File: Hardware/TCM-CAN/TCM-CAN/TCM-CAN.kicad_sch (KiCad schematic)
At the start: 1 part, among them J1 DTM13-12PA

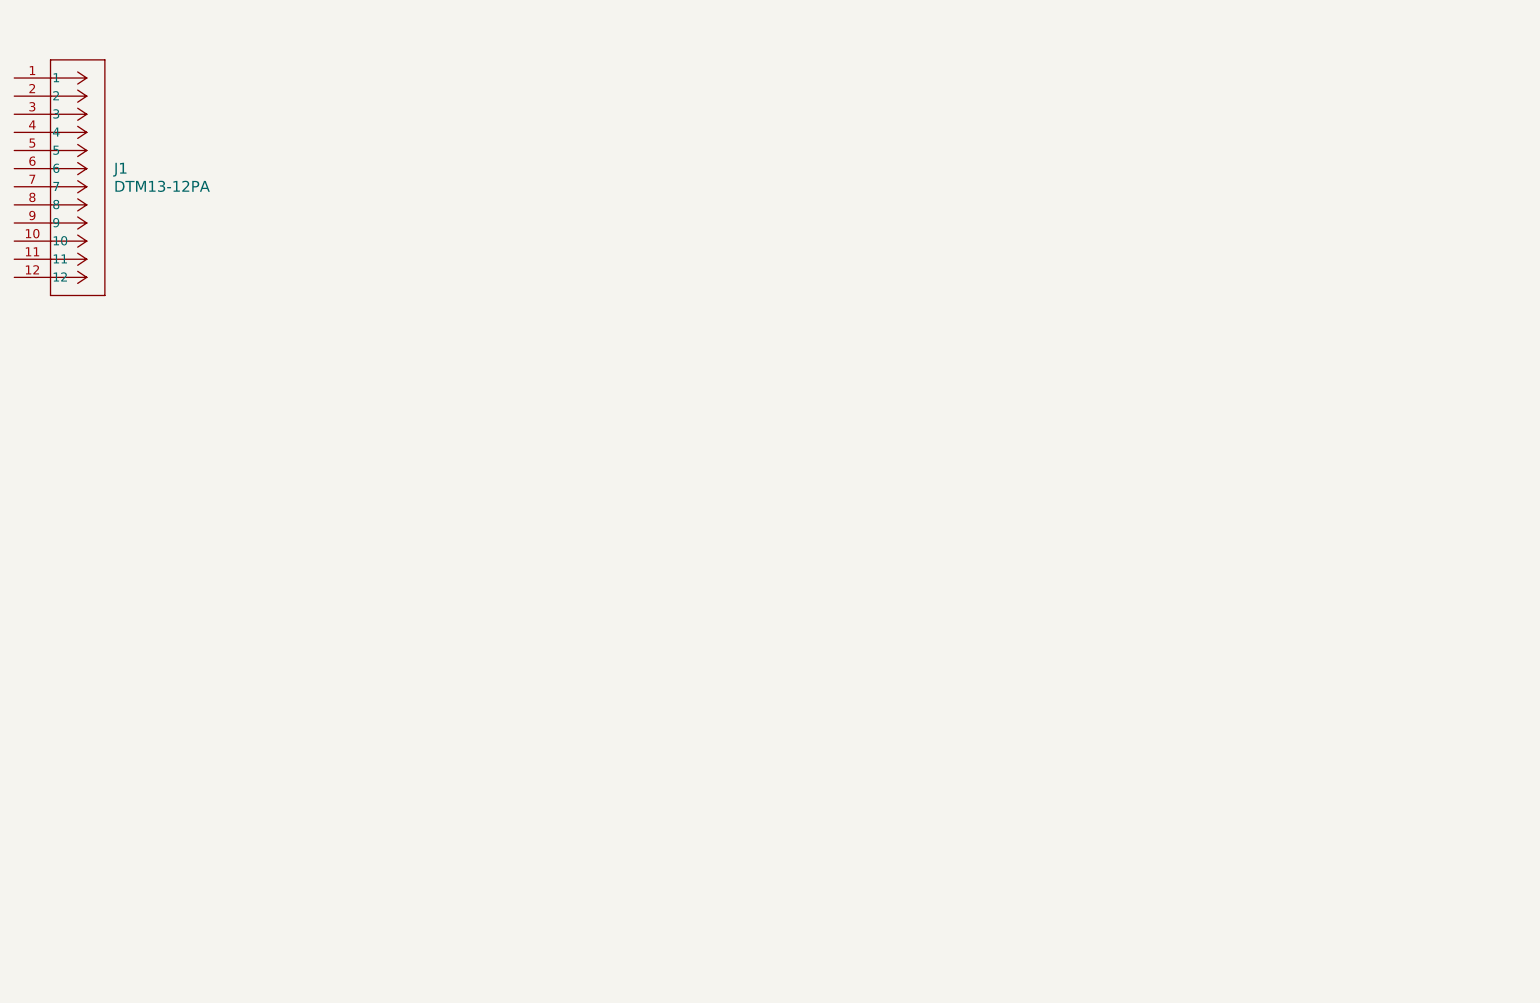
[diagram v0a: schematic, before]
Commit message: tcm can schematic done, only needs to be routed
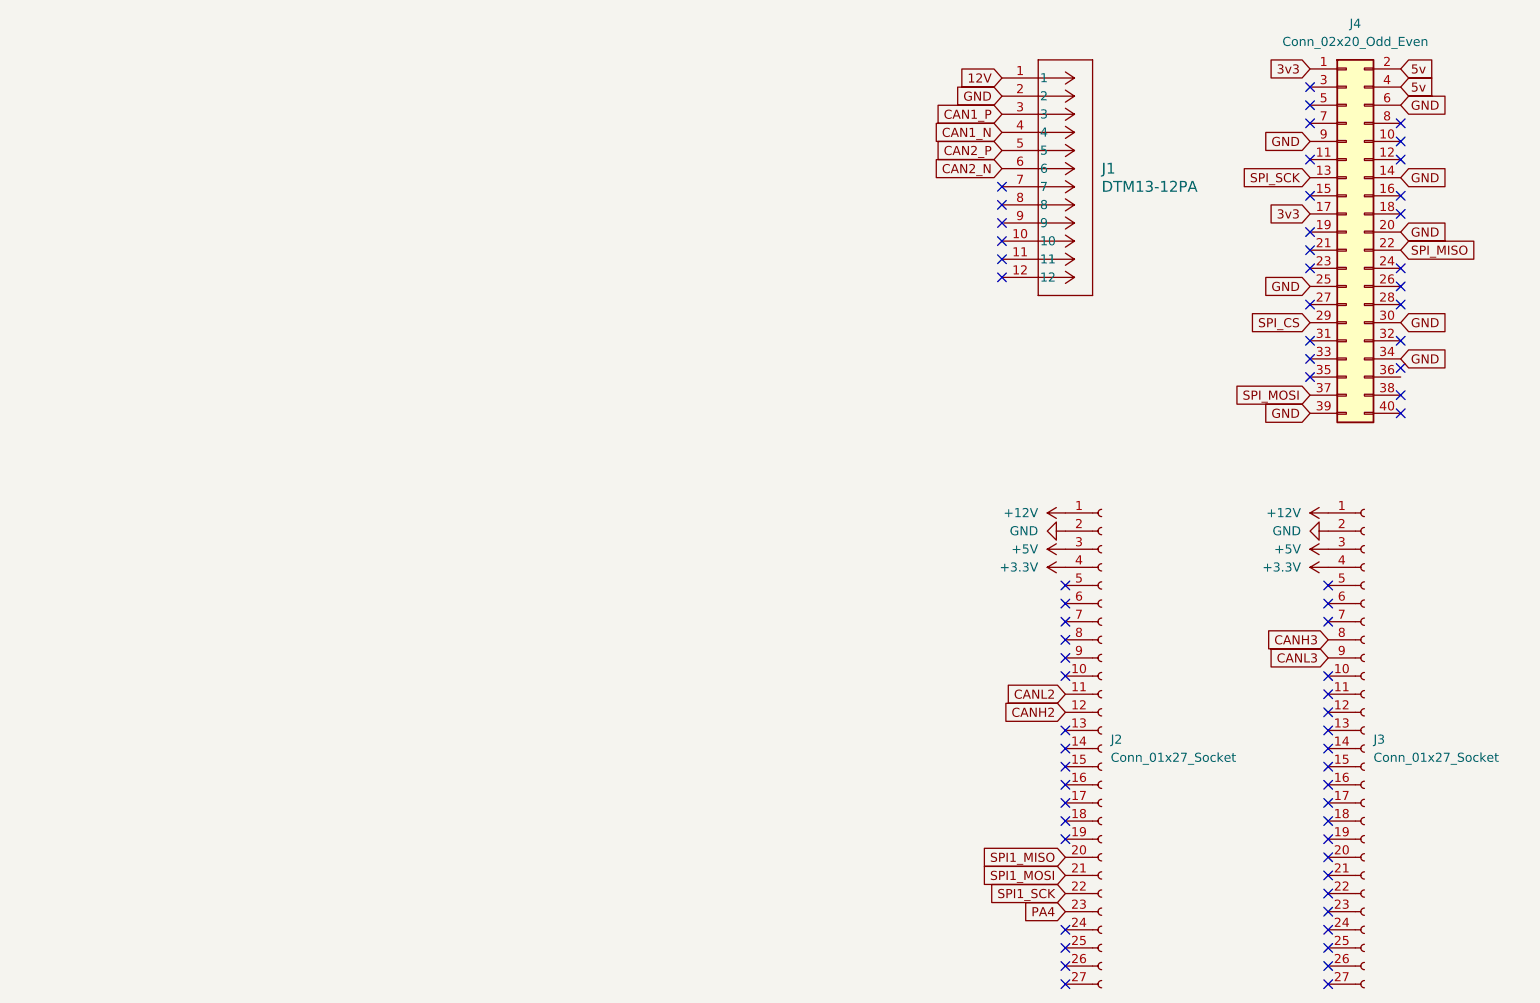
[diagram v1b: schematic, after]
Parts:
- added J2, J3: Conn_01x27_Socket, Connector_PinHeader_2.54mm:PinHeader_1x27_P2.54mm_Vertical, symbol Connector:Conn_01x27_Socket
- added J4: Conn_02x20_Odd_Even, Connector_PinSocket_2.54mm:PinSocket_2x20_P2.54mm_Vertical, symbol Connector_Generic:Conn_02x20_Odd_Even
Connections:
- net 12V: now reaches J1.1
- net GND: now reaches J1.2
- net GND: now also J2.2 (Pin_2), J3.2 (Pin_2), J4.14 (Pin_14), J4.20 (Pin_20), J4.25 (Pin_25), J4.30 (Pin_30), J4.34 (Pin_34), J4.39 (Pin_39), J4.6 (Pin_6), J4.9 (Pin_9)
- net CAN1_P: now reaches J1.3
- net CAN1_N: now reaches J1.4
- net CAN2_P: now reaches J1.5
- net CAN2_N: now reaches J1.6
- new net +12V: J2.1 (Pin_1), J3.1 (Pin_1)
- new net +3.3V: J2.4 (Pin_4), J3.4 (Pin_4)
- new net +5V: J2.3 (Pin_3), J3.3 (Pin_3)
- new net 3v3: J4.1 (Pin_1), J4.17 (Pin_17)
- new net 5v: J4.2 (Pin_2), J4.4 (Pin_4)
- new net CANH2: J2.12 (Pin_12)
- new net CANH3: J3.8 (Pin_8)
- new net CANL2: J2.11 (Pin_11)
- new net CANL3: J3.9 (Pin_9)
- new net PA4: J2.23 (Pin_23)
- new net SPI1_MISO: J2.20 (Pin_20)
- new net SPI1_MOSI: J2.21 (Pin_21)
- new net SPI1_SCK: J2.22 (Pin_22)
- new net SPI_CS: J4.29 (Pin_29)
- new net SPI_MISO: J4.22 (Pin_22)
- new net SPI_MOSI: J4.37 (Pin_37)
- new net SPI_SCK: J4.13 (Pin_13)
- no-connect marks 0 -> 68
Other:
- moved on the sheet: J1

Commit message: bug fix
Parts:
- removed J1: DTM13-12PA, CONN12_DTM13-12PA_TEC, symbol DTM:DTM13-12PA
- added J5: Conn_01x06_Socket, Connector_JST:JST_XH_B6B-XH-A_1x06_P2.50mm_Vertical, symbol Connector:Conn_01x06_Socket
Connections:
- net 12V: now also J5.1 (Pin_1)
- net CAN1_N: now also J5.4 (Pin_4)
- net CAN1_P: now also J5.3 (Pin_3)
- net CAN2_N: now also J5.6 (Pin_6)
- net CAN2_P: now also J5.5 (Pin_5)
- net GND: now also J5.2 (Pin_2)
- no-connect marks 68 -> 62
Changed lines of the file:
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@@
 	)
 	(no_connect
-		(at 171.45 36.83)
-	)
-	(no_connect
 		(at 227.33 62.23)
 	)
@@
 	)
 	(no_connect
-		(at 171.45 49.53)
-	)
-	(no_connect
 		(at 180.34 125.73)
 	)
@@
 	)
 	(no_connect
-		(at 171.45 41.91)
-	)
-	(no_connect
 		(at 217.17 113.03)
 	)
@@
 	)
 	(no_connect
-		(at 171.45 44.45)
-	)
-	(no_connect
 		(at 214.63 27.94)
 	)
@@
 	)
 	(no_connect
-		(at 171.45 39.37)
-	)
-	(no_connect
 		(at 227.33 38.1)
 	)
 	(no_connect
-		(at 171.45 46.99)
-	)
-	(no_connect
 		(at 217.17 138.43)
 	)
@@
 			"AAAAAAAAAAAAAAAAAAAAAAAAAAAAAAAAAAAAAAAAAAAAAAAAAAAAAAAAAAAAAAAAAAAAAAAAAAAA"
 			"AAAAAAAAAAAAAAAAAAAAAAAAAAAAAAAAAAAAAAAAAAAAAAAAAAAAAAAAAAAAAAAAAAAAAAAAAAAA"
-			"AAAAAAAAAAAAAAAAAAAAAAAAAAAAAAAAAAAAAAA="
+			"AAAAAAAAAAAAAAAAAAAAAAAAAAAAAAAAAAAAAAAAAAAAAAAAAAAAAAAAAAAAAAAAAAAAAAAAAAAA"
+			"AAAAAAAAAAAAAAAAAAAAAAAAAAAAAAAAAAAAAAAAAAAAAAAAAAAAAAAAAAAAAAAAAAAAAAAAAAAA"
+			"AAAAAAAAAAAAAAAAAAAAAAAAAAAAAAAAAAAAAAAAAAAAAAAAAAAAAAAAAAAAAAAAAAAAAAAAAAAA"
+			"AAAAAAAAAAAAAAAAAAAAAAAAAAAAAAAAAAAAAAAAAAAAAAAAAAAAAAAAAAAAAAAAAAAAAAAAAAAA"
+			"AAAAAAAAAAAAAAAAAAAAAAAAAAAAAAAAAAAAAAAAAAAAAAAAAAAAAAAAAAAAAAAAAAAAAAAAAAAA"
+			"AAAAAAAAAAAAAAAAAAAAAAAAAAAAAAAAAAAAAAAAAAAAAAAAAAAAAAAAAAAAAAAAAAAAAAAAAAAA"
+			"AAAAAAAAAAAAAAAAAAAAAAAAAAAAAAAAAAAAAAAAAAAAAAAAAAAAAAAAAAAAAAAAAAAAAAAAAAAA"
+			"AAAAAAAAAAAAAAAAAAAAAAAAAAAAAAAAAAAAAAAAAAAAAAAAAAAAAAAAAAAAAAAAAAAAAAAAAAAA"
+			"AAAAAAAAAAAAAAAAAAAAAAAAAAAAAAAAAAAAAAAAAAAAAAAAAAAAAAAAAAAAAAAAAAAAAAAAAAAA"
+			"AAAAAAAAAAAAAAAAAAAAAAAAAAAAAAAAAAAAAAAAAAAAAAAAAAAAAAAAAAAAAAAAAAAAAAAAAAAA"
+			"AAAAAAAAAAAAAAAAAAAAAAAAAAAAAAAAAAAAAAAAAAAAAAAAAAAAAAAAAAAAAAAAAAAAAAAAAAAA"
+			"AAAAAAAAAAAAAAAAAAAAAAAAAAAAAAAAAAAAAAAAAAAAAAAAAAAAAAAAAAAAAAAAAAAAAAAAAAAA"
+			"AAAAAAAAAAAAAAAAAAAAAAAAAAAAAAAAAAAAAAAAAAAAAAAAAAAAAAAAAAAAAAAAAAAAAAAAAAAA"
+			"AAAAAAAAAAAAAAAAAAAAAAAAAAAAAAAAAAAAAAAAAAAAAAAAAAAAAAAAAAAAAAAAAAAAAAAAAAAA"
+			"AAAAAAAAAAAAAAAAAAAAAAAAAAAAAAAAAAAAAAAAAAAAAAAAAAAAAAAAAAAAAAAAAAAAAAAAAAAA"
+			"AAAAAAAAAAAAAAAAAAAAAAAAAAAAAAAAAAAAAAAAAAAAAAAAAAAAAAAAAAAAAAAAAAAAAAAAAAAA"
+			"AAAAAAAAAAAAAAAAAAAAAAAAAAAAAAAAAAAAAAAAAAAAAAAAAAAAAAAAAAAAAAAAAAAAAAAAAAAA"
+			"AAAAAAAAAAAAAAAAAAAAAAAAAAAAAAAAAAAAAAAAAAAAAAAAAAAAAAAAAAAAAAAAAAAAAAAAAAAA"
+			"AAAAAAAAAAAAAAAAAAAAAAAAAAAAAAAAAAAAAA=="
 		)
 	)
@@
 		)
 	)
-	(global_label "3v3"
+	(global_label "CAN2_N"
 		(shape input)
-		(at 214.63 40.64 180)
+		(at 162.56 71.12 180)
 		(fields_autoplaced yes)
 		(effects
@@
 		)
 		(property "Intersheetrefs" "${INTERSHEET_REFS}"
-			(at 208.2582 40.64 0)
+			(at 152.3781 71.12 0)
 			(effects
 				(font
@@
 		)
 	)
-	(global_label "12V"
+	(global_label "CAN1_P"
+		(shape input)
+		(at 162.56 63.5 180)
+		(fields_autoplaced yes)
+		(effects
+			(font
+				(size 1.27 1.27)
+			)
+			(justify right)
+		)
+		(property "Intersheetrefs" "${INTERSHEET_REFS}"
+			(at 152.4386 63.5 0)
+			(effects
+				(font
+					(size 1.27 1.27)
+				)
+				(justify right)
+				(hide yes)
+			)
+		)
+	)
+	(global_label "3v3"
 		(shape input)
-		(at 171.45 21.59 180)
+		(at 214.63 40.64 180)
 		(fields_autoplaced yes)
 		(effects
@@
 		)
 		(property "Intersheetrefs" "${INTERSHEET_REFS}"
-			(at 164.9572 21.59 0)
+			(at 208.2582 40.64 0)
 			(effects
 				(font
@@
 	(global_label "GND"
 		(shape input)
-		(at 171.45 24.13 180)
+		(at 162.56 60.96 180)
 		(fields_autoplaced yes)
 		(effects
@@
 		)
 		(property "Intersheetrefs" "${INTERSHEET_REFS}"
-			(at 164.5943 24.13 0)
+			(at 155.7043 60.96 0)
 			(effects
 				(font
@@
 		)
 	)
-	(global_label "CAN2_P"
-		(shape input)
-		(at 171.45 31.75 180)
-		(fields_autoplaced yes)
-		(effects
-			(font
-				(size 1.27 1.27)
-			)
-			(justify right)
-		)
-		(property "Intersheetrefs" "${INTERSHEET_REFS}"
-			(at 161.3286 31.75 0)
-			(effects
-				(font
-					(size 1.27 1.27)
-				)
-				(justify right)
-				(hide yes)
-			)
-		)
-	)
 	(global_label "SPI_MOSI"
 		(shape input)
@@
 		)
 	)
-	(global_label "CAN1_P"
-		(shape input)
-		(at 171.45 26.67 180)
-		(fields_autoplaced yes)
-		(effects
-			(font
-				(size 1.27 1.27)
-			)
-			(justify right)
-		)
-		(property "Intersheetrefs" "${INTERSHEET_REFS}"
-			(at 161.3286 26.67 0)
-			(effects
-				(font
-					(size 1.27 1.27)
-				)
-				(justify right)
-				(hide yes)
-			)
-		)
-	)
-	(global_label "CAN2_N"
+	(global_label "CAN1_N"
 		(shape input)
-		(at 171.45 34.29 180)
+		(at 162.56 66.04 180)
 		(fields_autoplaced yes)
 		(effects
@@
 		)
 		(property "Intersheetrefs" "${INTERSHEET_REFS}"
-			(at 161.2681 34.29 0)
+			(at 152.3781 66.04 0)
 			(effects
 				(font
@@
 		)
 	)
-	(global_label "CAN1_N"
+	(global_label "PA4"
 		(shape input)
-		(at 171.45 29.21 180)
+		(at 180.34 138.43 180)
 		(fields_autoplaced yes)
 		(effects
@@
 		)
 		(property "Intersheetrefs" "${INTERSHEET_REFS}"
-			(at 161.2681 29.21 0)
+			(at 173.7867 138.43 0)
 			(effects
 				(font
@@
 		)
 	)
-	(global_label "PA4"
+	(global_label "SPI1_SCK"
 		(shape input)
-		(at 180.34 138.43 180)
+		(at 180.34 135.89 180)
 		(fields_autoplaced yes)
 		(effects
@@
 		)
 		(property "Intersheetrefs" "${INTERSHEET_REFS}"
-			(at 173.7867 138.43 0)
+			(at 168.3439 135.89 0)
 			(effects
 				(font
@@
 		)
 	)
-	(global_label "SPI1_SCK"
+	(global_label "CAN2_P"
 		(shape input)
-		(at 180.34 135.89 180)
+		(at 162.56 68.58 180)
 		(fields_autoplaced yes)
 		(effects
@@
 		)
 		(property "Intersheetrefs" "${INTERSHEET_REFS}"
-			(at 168.3439 135.89 0)
+			(at 152.4386 68.58 0)
 			(effects
 				(font
@@
 		)
 	)
-	(global_label "GND"
+	(global_label "12V"
 		(shape input)
-		(at 214.63 30.48 180)
+		(at 162.56 58.42 180)
 		(fields_autoplaced yes)
 		(effects
@@
 		)
 		(property "Intersheetrefs" "${INTERSHEET_REFS}"
-			(at 207.7743 30.48 0)
+			(at 156.0672 58.42 0)
 			(effects
 				(font
@@
 	(global_label "GND"
 		(shape input)
-		(at 227.33 43.18 0)
+		(at 214.63 30.48 180)
 		(fields_autoplaced yes)
 		(effects
@@
 				(size 1.27 1.27)
 			)
-			(justify left)
+			(justify right)
 		)
 		(property "Intersheetrefs" "${INTERSHEET_REFS}"
-			(at 234.1857 43.18 0)
+			(at 207.7743 30.48 0)
 			(effects
 				(font
 					(size 1.27 1.27)
 				)
-				(justify left)
+				(justify right)
 				(hide yes)
 			)
 		)
 	)
-	(symbol
-		(lib_id "DTM:DTM13-12PA")
-		(at 181.61 36.83 0)
-		(unit 1)
-		(exclude_from_sim no)
-		(in_bom yes)
-		(on_board yes)
-		(dnp no)
+	(global_label "GND"
+		(shape input)
+		(at 227.33 43.18 0)
 		(fields_autoplaced yes)
-		(property "Reference" "J1"
-			(at 185.42 34.2899 0)
-			(effects
-				(font
-					(size 1.524 1.524)
-				)
-				(justify left)
-			)
-		)
-		(property "Value" "DTM13-12PA"
-			(at 185.42 36.8299 0)
-			(effects
-				(font
-					(size 1.524 1.524)
-				)
-				(justify left)
-			)
-		)
-		(property "Footprint" "CONN12_DTM13-12PA_TEC"
-			(at 181.61 36.83 0)
-			(effects
-				(font
-					(size 1.27 1.27)
-					(italic yes)
-				)
-				(hide yes)
-			)
-		)
-		(property "Datasheet" "DTM13-12PA"
-			(at 181.61 36.83 0)
-			(effects
-				(font
-					(size 1.27 1.27)
-					(italic yes)
-				)
-				(hide yes)
+		(effects
+			(font
+				(size 1.27 1.27)
 			)
+			(justify left)
 		)
-		(property "Description" ""
-			(at 181.61 36.83 0)
+		(property "Intersheetrefs" "${INTERSHEET_REFS}"
+			(at 234.1857 43.18 0)
 			(effects
 				(font
 					(size 1.27 1.27)
 				)
+				(justify left)
 				(hide yes)
 			)
 		)
-		(pin "8"
-		)
-		(pin "3"
-		)
-		(pin "6"
-		)
-		(pin "4"
-		)
-		(pin "1"
-		)
-		(pin "12"
-		)
-		(pin "10"
-		)
-		(pin "5"
-		)
-		(pin "9"
-		)
-		(pin "2"
-		)
-		(pin "7"
-		)
-		(pin "11"
-		)
-		(instances
-			(project ""
-				(path "/dce5d582-08ac-45e6-8e98-75b83df6efb2"
-					(reference "J1")
-					(unit 1)
-				)
-			)
-		)
 	)
 	(symbol
@@
 					(unit 1)
 				)
+			)
+		)
+	)
+	(symbol
+		(lib_id "Connector:Conn_01x06_Socket")
+		(at 167.64 63.5 0)
+		(unit 1)
+		(exclude_from_sim no)
+		(in_bom yes)
+		(on_board yes)
+		(dnp no)
+		(fields_autoplaced yes)
+		(property "Reference" "J5"
+			(at 168.91 63.4999 0)
+			(effects
+				(font
+					(size 1.27 1.27)
+				)
+				(justify left)
+			)
+		)
+		(property "Value" "Conn_01x06_Socket"
+			(at 168.91 66.0399 0)
+			(effects
+				(font
+					(size 1.27 1.27)
+				)
+				(justify left)
+			)
+		)
+		(property "Footprint" "Connector_JST:JST_XH_B6B-XH-A_1x06_P2.50mm_Vertical"
+			(at 167.64 63.5 0)
+			(effects
+				(font
+					(size 1.27 1.27)
+				)
+				(hide yes)
+			)
+		)
+		(property "Datasheet" "~"
+			(at 167.64 63.5 0)
+			(effects
+				(font
+					(size 1.27 1.27)
+				)
+				(hide yes)
+			)
+		)
+		(property "Description" "Generic connector, single row, 01x06, script generated"
+			(at 167.64 63.5 0)
+			(effects
+				(font
+					(size 1.27 1.27)
+				)
+				(hide yes)
+			)
+		)
+		(pin "1"
+		)
+		(pin "6"
+		)
+		(pin "5"
+		)
+		(pin "4"
+		)
+		(pin "2"
+		)
+		(pin "3"
+		)
+		(instances
+			(project ""
+				(path "/dce5d582-08ac-45e6-8e98-75b83df6efb2"
+					(reference "J5")
+					(unit 1)
+				)
